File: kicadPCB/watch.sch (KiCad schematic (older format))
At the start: 62 parts, among them IC1 ISL1209, J1 USB_OTG, M1 BOS_LIBS_SWD_BREAKOUTS, Q1 Q_PNP_CEB, T1 BC850, U2 MKL27Z256VLH4, Y1 Crystal

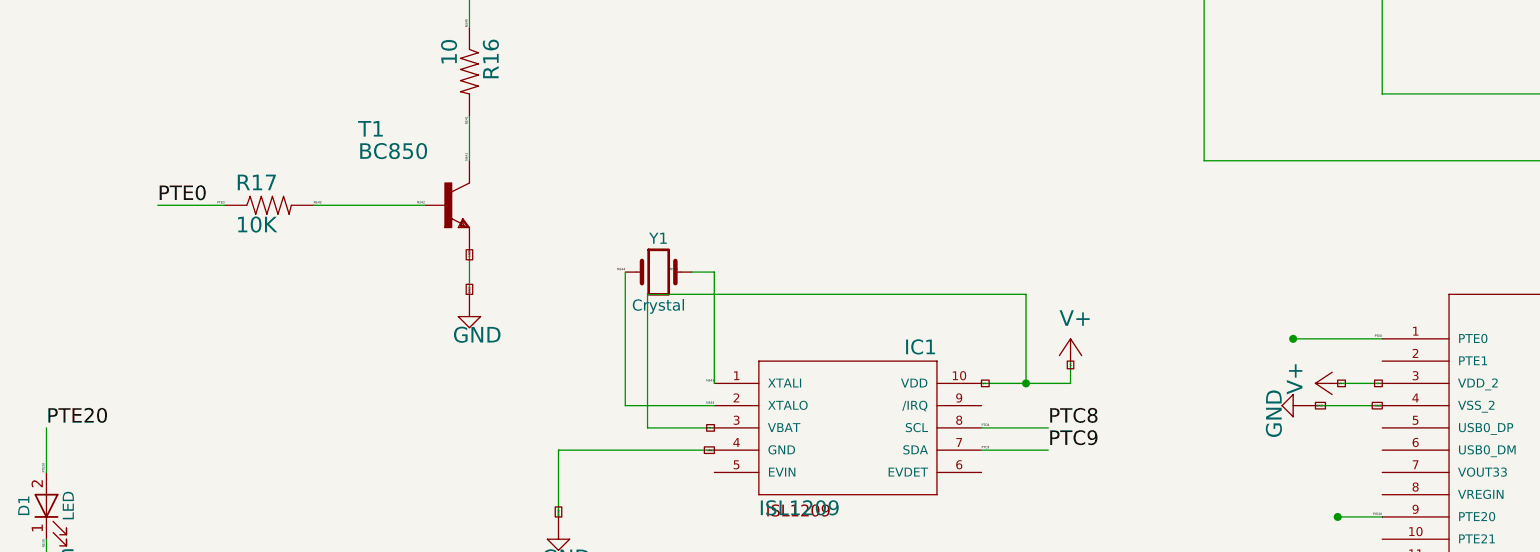
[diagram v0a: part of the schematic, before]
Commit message: fixed Laser npn, fixed laser and led south from bridge
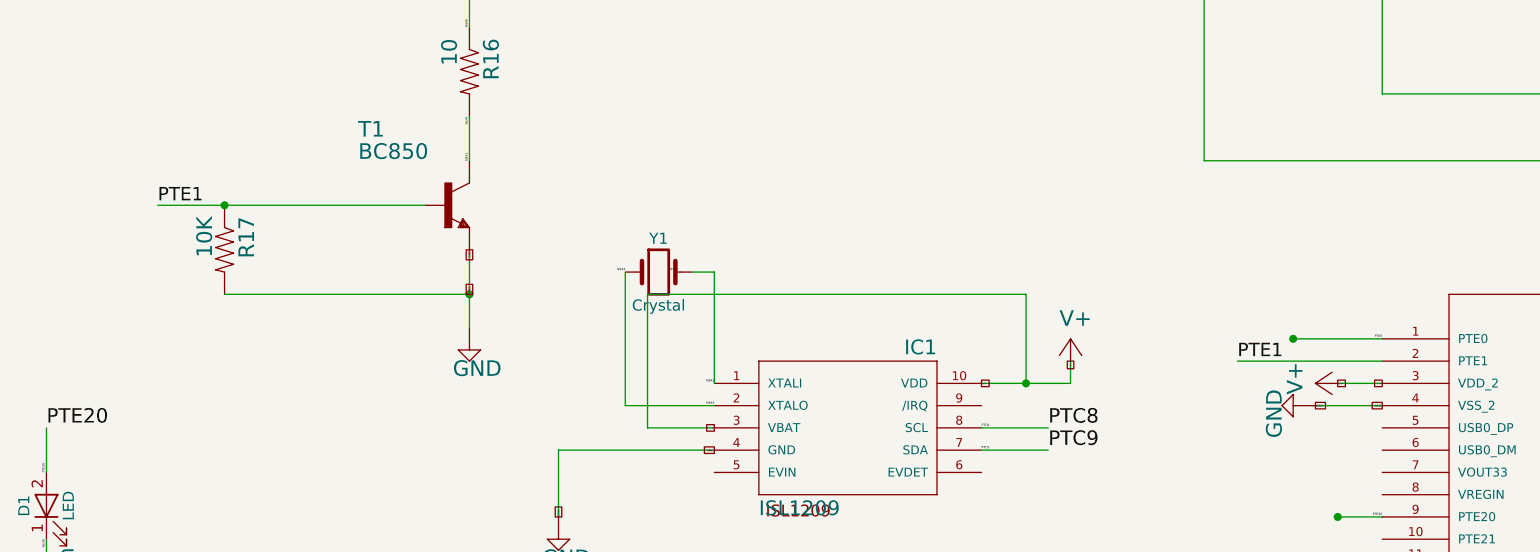
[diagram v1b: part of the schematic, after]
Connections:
- net labels added: PTE1
- net labels removed: N$42
- wire segments 264 -> 265
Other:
- moved on the sheet: R17
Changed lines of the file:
@@
 L SPARKFUN-RESISTORS_RESISTOR R17
 U 1 1 58A20105
-P 5150 7450
-F 0 "R17" H 5000 7509 70  0000 L BNN
-F 1 "10K" H 5000 7320 70  0000 L BNN
-F 2 "watch:SPARKFUN-RESISTORS_0603-RES" H 5140 7240 65  0001 L TNN
-F 3 "" H 5150 7450 60  0001 C CNN
-	1    5150 7450
-	1    0    0    -1
+P 4950 7650
+F 0 "R17" H 4800 7709 70  0000 L BNN
+F 1 "10K" H 4800 7520 70  0000 L BNN
+F 2 "watch:SPARKFUN-RESISTORS_0603-RES" H 4940 7440 65  0001 L TNN
+F 3 "" H 4950 7650 60  0001 C CNN
+	1    4950 7650
+	0    1    1    0
 $EndComp
 $Comp
@@
 L SUPPLY2_GND #SUPPLY030
 U 1 1 58A211D1
-P 6050 7950
-F 0 "#SUPPLY030" H 5975 7825 70  0001 L BNN
-F 1 "GND" H 5975 7825 70  0000 L BNN
-F 2 "" H 6050 7950 60  0001 C CNN
-F 3 "" H 6050 7950 60  0001 C CNN
-	1    6050 7950
+P 6050 8100
+F 0 "#SUPPLY030" H 5975 7975 70  0001 L BNN
+F 1 "GND" H 5975 7975 70  0000 L BNN
+F 2 "" H 6050 8100 60  0001 C CNN
+F 3 "" H 6050 8100 60  0001 C CNN
+	1    6050 8100
 	1    0    0    -1
 $EndComp
@@
 Text Label 4050 10850 0    65   ~ 0
 PTD5
-Text Label 4650 7450 0    65   ~ 0
-PTE0
 Text Label 4150 8450 0    65   ~ 0
 PTE20
@@
 Text Label 6050 7050 3    10   ~ 0
 N$41
-Text Label 5350 7450 0    10   ~ 0
-N$42
-Text Label 5850 7450 2    10   ~ 0
-N$42
 Text Label 6950 7750 0    10   ~ 0
 N$43
@@
 Text Label 4050 11150 1    10   ~ 0
 PTD5
-Text Label 4950 7450 2    10   ~ 0
-PTE0
 Text Label 10150 8050 2    10   ~ 0
 PTE0
@@
 	4150 9450 4150 9650
 Wire Wire Line
-	6050 7650 6050 7850
+	6050 7650 6050 8000
 Wire Wire Line
 	15800 10450 15900 10450
@@
 	6050 7250 6050 7050
 Wire Wire Line
-	5350 7450 5850 7450
+	4650 7450 5850 7450
 Wire Wire Line
 	7150 7750 7150 8250
@@
 Wire Wire Line
 	4050 11150 4050 10850
-Wire Wire Line
-	4950 7450 4650 7450
 Wire Wire Line
 	10150 8050 9750 8050
@@
 Wire Wire Line
 	16650 9700 16350 9700
+Wire Wire Line
+	4950 7850 6050 7850
+Connection ~ 6050 7850
+Connection ~ 4950 7450
+Wire Wire Line
+	9500 8150 10150 8150
+Text Label 9500 8150 0    60   ~ 0
+PTE1
+Text Label 4650 7450 0    60   ~ 0
+PTE1
 $EndSCHEMATC

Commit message: added pnp resistor
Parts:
- added R18: 330k, Resistor_SMD:R_0603_1608Metric, symbol Device:R
- 12CR2, GPTX46, I2CR1, R1, R10, R11, R12, R13, R14, R15, R16, R17, R2, R26, R27, R29, R3, R30, R4, R5, R6, R7, R8, R9: symbol SPARKFUN-RESISTORS_RESISTOR -> watch:SPARKFUN-RESISTORS_RESISTOR
- C1, C2, C5, C6, C7, C8, C9, COMPCAP46: symbol SPARKFUN_CAP -> watch:SPARKFUN_CAP
- C3, C4: symbol SPARKFUN-CAPACITORS_0.1UF-25V_+80_-20%__0603_ -> watch:SPARKFUN-CAPACITORS_0.1UF-25V_+80_-20%__0603_
- D1, D2, D3, D4, D5: symbol LED -> watch-rescue:LED
- DISP1, DISP2: symbol SPARKFUN-DISPLAYS_7-SEGMENT-4DIGIT-COUNTER -> watch:SPARKFUN-DISPLAYS_7-SEGMENT-4DIGIT-COUNTER
- IC1: symbol ADAFRUIT_ISL1209 -> watch:ADAFRUIT_ISL1209
- J1: symbol USB_OTG -> watch-rescue:USB_OTG
- LASER46: symbol PHOTONICS_LD -> watch:PHOTONICS_LD
- LED1: symbol EAGLE-LTSPICE_LED_E -> watch:EAGLE-LTSPICE_LED_E
- LIPO46: symbol SPARKFUN-CONNECTORS_JST_2MM_MALE -> watch:SPARKFUN-CONNECTORS_JST_2MM_MALE
- LS1: symbol Speaker -> watch-rescue:Speaker
- M1: symbol BOS_LIBS_SWD_BREAKOUTS -> watch:BOS_LIBS_SWD_BREAKOUTS
- Q1: symbol Q_PNP_BEC -> watch-rescue:Q_PNP_BEC
- S11: symbol ADAFRUIT_EG1213 -> watch:ADAFRUIT_EG1213
- T1: symbol TRANSISTOR_BC850 -> watch:TRANSISTOR_BC850
- U$1: symbol SPARKFUN_HMC6343 -> watch:SPARKFUN_HMC6343
- U$2: symbol GEEKAMMO_MCP73831 -> watch:GEEKAMMO_MCP73831
- U$3, U$7, U$8, U$9: symbol BOS_LIBS_DIPS -> watch:BOS_LIBS_DIPS
- U$4, U$5: symbol BOS_LIBS_74HC595PW -> watch:BOS_LIBS_74HC595PW
- U1: symbol ADAFRUIT_GPS_FGPMMOPA6H -> watch:ADAFRUIT_GPS_FGPMMOPA6H
- U2: symbol FREESCALE_MKL27Z256VLH4 -> watch:FREESCALE_MKL27Z256VLH4
- Y1: symbol Crystal -> watch-rescue:Crystal
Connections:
- wire segments 265 -> 310
